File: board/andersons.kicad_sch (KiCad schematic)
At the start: 4 parts

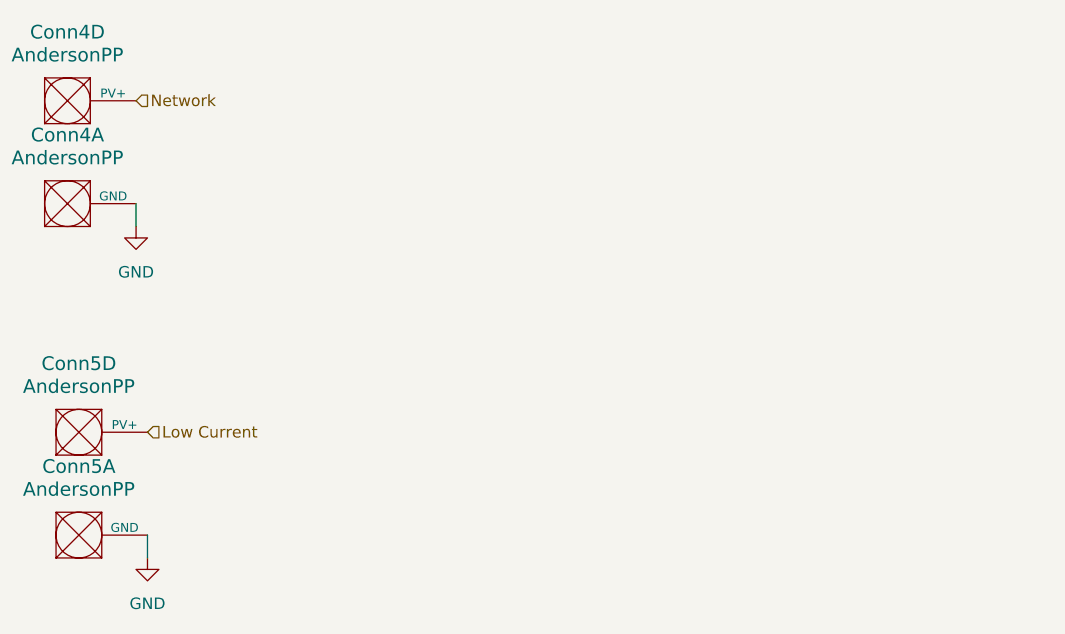
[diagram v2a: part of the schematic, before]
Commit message: include andersons for all LC and teensy enables for m2, m5, and m9
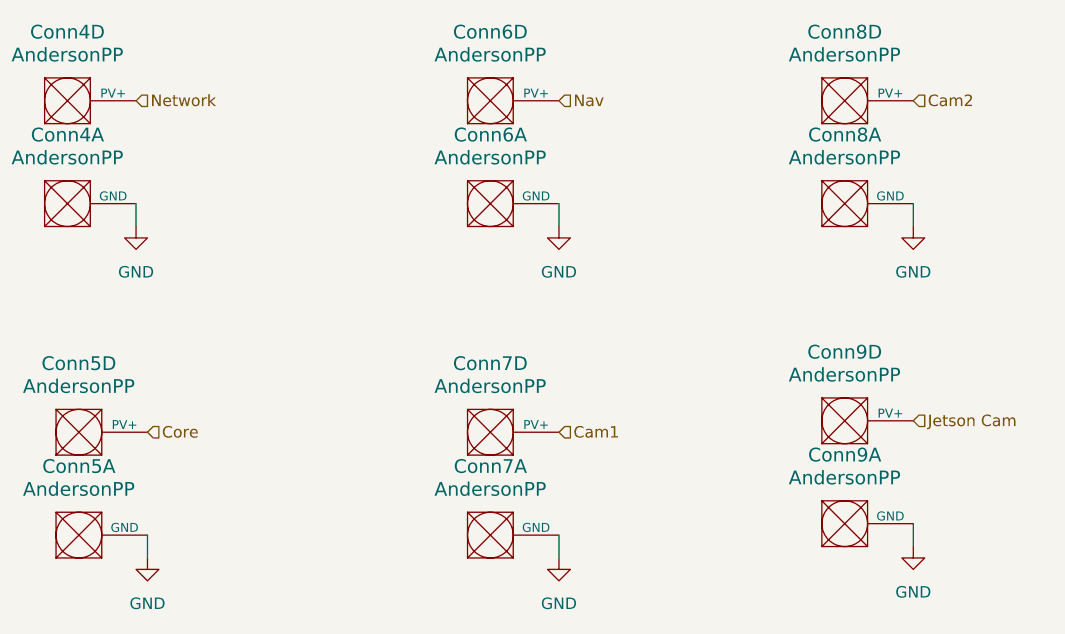
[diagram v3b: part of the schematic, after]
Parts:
- added Conn6, Conn7, Conn8, Conn9: AndersonPP, symbol MRDT_Connectors:AndersonPP
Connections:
- net GND: now also Conn6.1 (GND), Conn7.1 (GND), Conn8.1 (GND), Conn9.1 (GND)
- net Low Current renamed Core
- new net Cam1: Conn7.4 (PV+)
- new net Cam2: Conn8.4 (PV+)
- new net Jetson Cam: Conn9.4 (PV+)
- new net Nav: Conn6.4 (PV+)

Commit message: anderson footprints
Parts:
- Conn2, Conn3, Conn4, Conn5, Conn6, Conn7, Conn8, Conn9: footprint (none) -> MRDT_Connectors:Square_Anderson_2_H_Side_By_Side_PV
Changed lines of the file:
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@@
 			)
 		)
-		(property "Footprint" ""
+		(property "Footprint" "MRDT_Connectors:Square_Anderson_2_H_Side_By_Side_PV"
 			(at 147.32 68.58 0)
 			(effects
@@
 			)
 		)
-		(property "Footprint" ""
+		(property "Footprint" "MRDT_Connectors:Square_Anderson_2_H_Side_By_Side_PV"
 			(at 147.32 105.41 0)
 			(effects
@@
 			)
 		)
-		(property "Footprint" ""
+		(property "Footprint" "MRDT_Connectors:Square_Anderson_2_H_Side_By_Side_PV"
 			(at 36.83 57.15 0)
 			(effects
@@
 			)
 		)
-		(property "Footprint" ""
+		(property "Footprint" "MRDT_Connectors:Square_Anderson_2_H_Side_By_Side_PV"
 			(at 100.33 57.15 0)
 			(effects
@@
 			)
 		)
-		(property "Footprint" ""
+		(property "Footprint" "MRDT_Connectors:Square_Anderson_2_H_Side_By_Side_PV"
 			(at 186.69 92.71 0)
 			(effects
@@
 			)
 		)
-		(property "Footprint" ""
+		(property "Footprint" "MRDT_Connectors:Square_Anderson_2_H_Side_By_Side_PV"
 			(at 101.6 105.41 0)
 			(effects
@@
 			)
 		)
-		(property "Footprint" ""
+		(property "Footprint" "MRDT_Connectors:Square_Anderson_2_H_Side_By_Side_PV"
 			(at 38.1 93.98 0)
 			(effects
@@
 			)
 		)
-		(property "Footprint" ""
+		(property "Footprint" "MRDT_Connectors:Square_Anderson_2_H_Side_By_Side_PV"
 			(at 101.6 93.98 0)
 			(effects
@@
 			)
 		)
-		(property "Footprint" ""
+		(property "Footprint" "MRDT_Connectors:Square_Anderson_2_H_Side_By_Side_PV"
 			(at 186.69 104.14 0)
 			(effects
@@
 			)
 		)
-		(property "Footprint" ""
+		(property "Footprint" "MRDT_Connectors:Square_Anderson_2_H_Side_By_Side_PV"
 			(at 147.32 93.98 0)
 			(effects
@@
 			)
 		)
-		(property "Footprint" ""
+		(property "Footprint" "MRDT_Connectors:Square_Anderson_2_H_Side_By_Side_PV"
 			(at 147.32 57.15 0)
 			(effects
@@
 			)
 		)
-		(property "Footprint" ""
+		(property "Footprint" "MRDT_Connectors:Square_Anderson_2_H_Side_By_Side_PV"
 			(at 100.33 68.58 0)
 			(effects
@@
 			)
 		)
-		(property "Footprint" ""
+		(property "Footprint" "MRDT_Connectors:Square_Anderson_2_H_Side_By_Side_PV"
 			(at 186.69 68.58 0)
 			(effects
@@
 			)
 		)
-		(property "Footprint" ""
+		(property "Footprint" "MRDT_Connectors:Square_Anderson_2_H_Side_By_Side_PV"
 			(at 36.83 68.58 0)
 			(effects
@@
 			)
 		)
-		(property "Footprint" ""
+		(property "Footprint" "MRDT_Connectors:Square_Anderson_2_H_Side_By_Side_PV"
 			(at 186.69 57.15 0)
 			(effects
@@
 			)
 		)
-		(property "Footprint" ""
+		(property "Footprint" "MRDT_Connectors:Square_Anderson_2_H_Side_By_Side_PV"
 			(at 38.1 105.41 0)
 			(effects

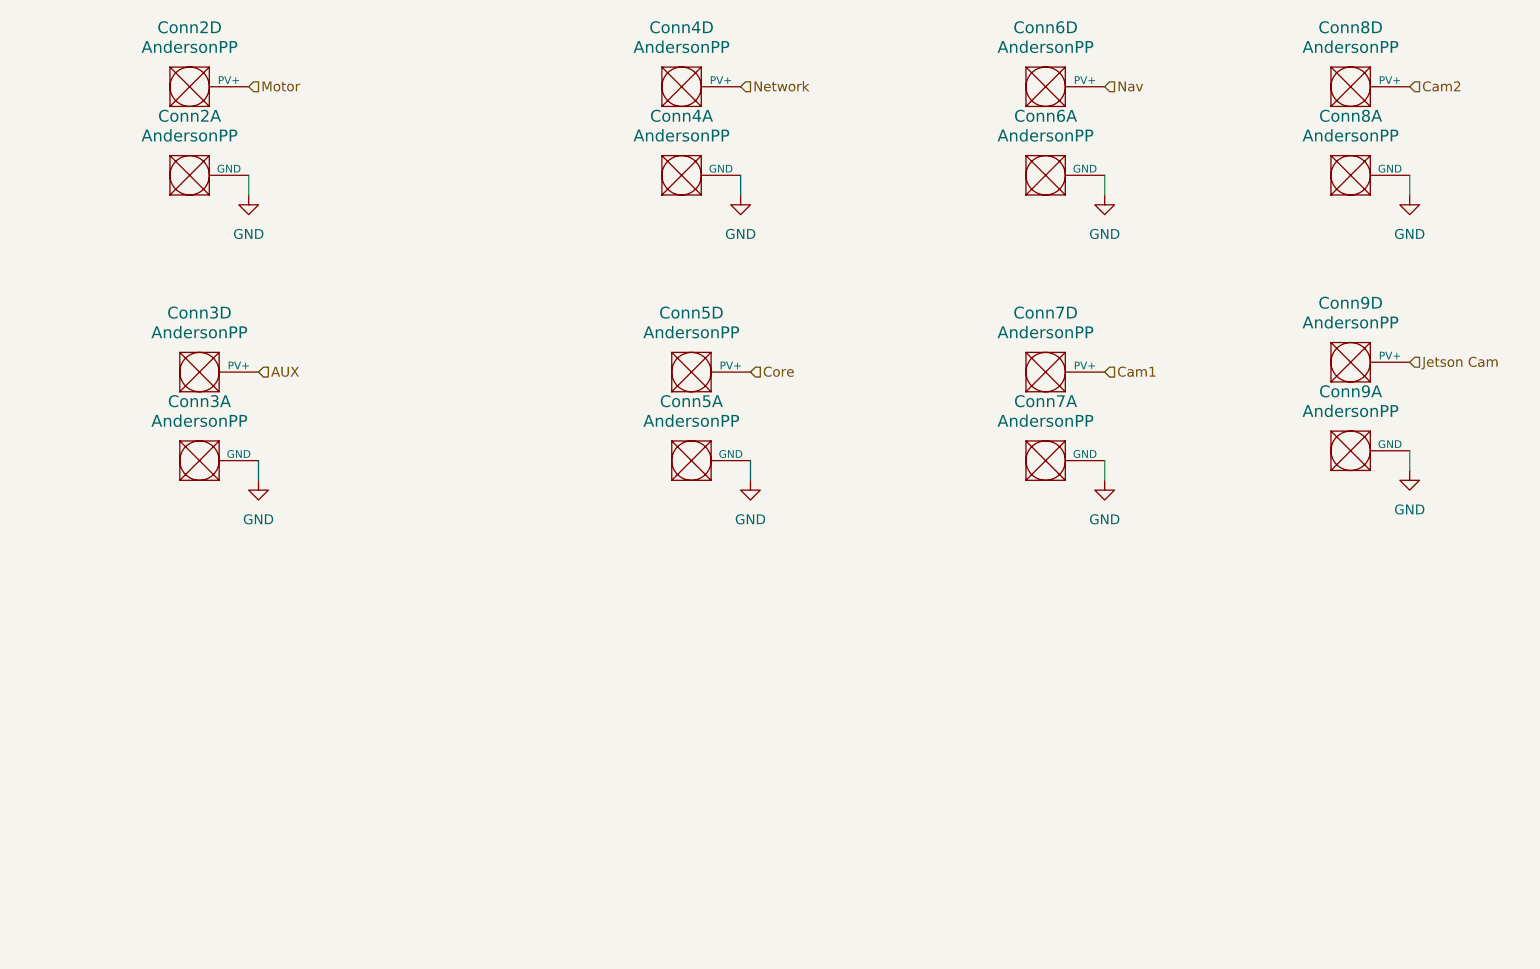
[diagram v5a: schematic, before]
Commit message: new connectors
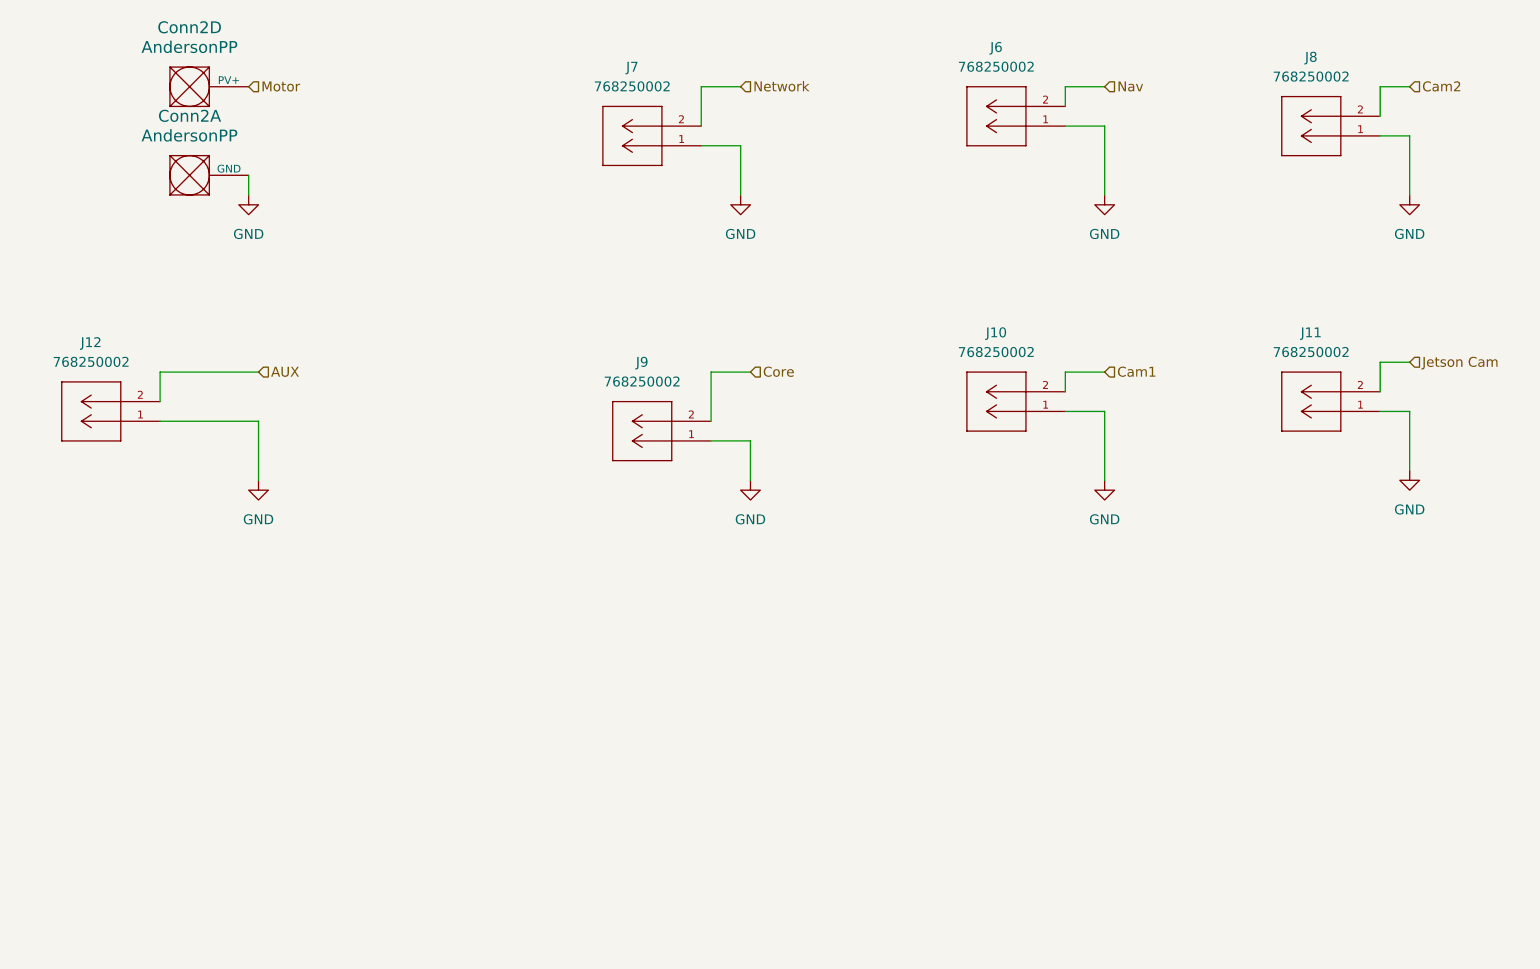
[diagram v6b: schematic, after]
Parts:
- removed Conn3, Conn4, Conn5, Conn6, Conn7, Conn8, Conn9: AndersonPP, MRDT_Connectors:Square_Anderson_2_H_Side_By_Side_PV, symbol MRDT_Connectors:AndersonPP
- added J10, J11, J12, J6, J7, J8, J9: 768250002, 768250002:CONN_SD-76825-0100_02_MOL, symbol PowerManagementBoard:768250002
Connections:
- net AUX: now also J12.2
- net Cam1: now also J10.2
- net Cam2: now also J8.2
- net Core: now also J9.2
- net GND: now also J10.1, J11.1, J12.1, J6.1, J7.1, J8.1, J9.1
- net Jetson Cam: now also J11.2
- net Nav: now also J6.2
- net Network: now also J7.2

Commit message: PCB start
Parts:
- J10, J11, J12, J6, J7, J8, J9: footprint 768250002:CONN_SD-76825-0100_02_MOL -> PowerManagementBoard:CONN_SD-76825-0100_02_MOL
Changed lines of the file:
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@@
+	(wire
+		(pts
+			(xy 52.07 83.82) (xy 52.07 91.44)
+		)
+		(stroke
+			(width 0)
+			(type default)
+		)
+	)
+	(wire
+		(pts
+			(xy 50.8 52.07) (xy 50.8 54.61)
+		)
+		(stroke
+			(width 0)
+			(type default)
+		)
+	)
+	(wire
+		(pts
+			(xy 200.66 40.64) (xy 196.85 40.64)
+		)
+		(stroke
+			(width 0)
+			(type default)
+		)
+	)
+	(wire
+		(pts
+			(xy 161.29 77.47) (xy 156.21 77.47)
+		)
+		(stroke
+			(width 0)
+			(type default)
+		)
+	)
 	(wire
 		(pts
@@
 	(wire
 		(pts
-			(xy 52.07 83.82) (xy 52.07 91.44)
-		)
-		(stroke
-			(width 0)
-			(type default)
-		)
-	)
-	(wire
-		(pts
-			(xy 50.8 52.07) (xy 50.8 54.61)
-		)
-		(stroke
-			(width 0)
-			(type default)
-		)
-	)
-	(wire
-		(pts
-			(xy 200.66 40.64) (xy 196.85 40.64)
-		)
-		(stroke
-			(width 0)
-			(type default)
-		)
-	)
-	(wire
-		(pts
-			(xy 161.29 77.47) (xy 156.21 77.47)
-		)
-		(stroke
-			(width 0)
-			(type default)
-		)
-	)
-	(wire
-		(pts
 			(xy 161.29 40.64) (xy 156.21 40.64)
 		)
@@
 	(wire
 		(pts
+			(xy 196.85 76.2) (xy 196.85 80.01)
+		)
+		(stroke
+			(width 0)
+			(type default)
+		)
+	)
+	(wire
+		(pts
+			(xy 53.34 40.64) (xy 50.8 40.64)
+		)
+		(stroke
+			(width 0)
+			(type default)
+		)
+	)
+	(wire
+		(pts
 			(xy 109.22 40.64) (xy 109.22 45.72)
 		)
@@
 		(pts
 			(xy 114.3 48.26) (xy 114.3 54.61)
-		)
-		(stroke
-			(width 0)
-			(type default)
-		)
-	)
-	(wire
-		(pts
-			(xy 196.85 76.2) (xy 196.85 80.01)
 		)
 		(stroke
@@
 	(hierarchical_label "Motor"
 		(shape input)
-		(at 50.8 40.64 0)
+		(at 53.34 40.64 0)
 		(effects
 			(font
@@
 			)
 		)
-		(property "Footprint" "768250002:CONN_SD-76825-0100_02_MOL"
+		(property "Footprint" "PowerManagementBoard:CONN_SD-76825-0100_02_MOL"
 			(at 156.21 45.72 0)
 			(effects
@@
 			)
 		)
-		(property "Footprint" "768250002:CONN_SD-76825-0100_02_MOL"
+		(property "Footprint" "PowerManagementBoard:CONN_SD-76825-0100_02_MOL"
 			(at 109.22 48.26 0)
 			(effects
@@
 			)
 		)
-		(property "Footprint" "768250002:CONN_SD-76825-0100_02_MOL"
+		(property "Footprint" "PowerManagementBoard:CONN_SD-76825-0100_02_MOL"
 			(at 39.37 83.82 0)
 			(effects
@@
 			)
 		)
-		(property "Footprint" "768250002:CONN_SD-76825-0100_02_MOL"
+		(property "Footprint" "PowerManagementBoard:CONN_SD-76825-0100_02_MOL"
 			(at 110.49 86.36 0)
 			(effects
@@
 			)
 		)
-		(property "Footprint" "768250002:CONN_SD-76825-0100_02_MOL"
+		(property "Footprint" "PowerManagementBoard:CONN_SD-76825-0100_02_MOL"
 			(at 196.85 46.99 0)
 			(effects
@@
 			)
 		)
-		(property "Footprint" "768250002:CONN_SD-76825-0100_02_MOL"
+		(property "Footprint" "PowerManagementBoard:CONN_SD-76825-0100_02_MOL"
 			(at 156.21 82.55 0)
 			(effects
@@
 			)
 		)
-		(property "Footprint" "768250002:CONN_SD-76825-0100_02_MOL"
+		(property "Footprint" "PowerManagementBoard:CONN_SD-76825-0100_02_MOL"
 			(at 196.85 82.55 0)
 			(effects

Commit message: Board before M5 Kill
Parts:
- removed Conn2: AndersonPP, MRDT_Connectors:Square_Anderson_2_H_Side_By_Side_PV, symbol MRDT_Connectors:AndersonPP
- added J13, J14, J15, J16, J17, J18: 768250002, PowerManagementBoard:CONN_SD-76825-0100_02_MOL, symbol PowerManagementBoard:768250002
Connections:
- net GND: now also J13.1, J14.1, J15.1, J16.1, J17.1, J18.1
- net Motor: now also J13.2, J14.2, J15.2, J16.2, J17.2, J18.2
